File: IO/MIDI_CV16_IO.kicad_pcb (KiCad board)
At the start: 2 copper layers, 59.5 x 99.5 mm, 111 parts, among them J1 Conn_01x08_Male, J10 AudioJack2_SwitchT, J11 Conn_01x10_Male, J12 AudioJack2_SwitchT, J13 AudioJack2_SwitchT, J14 AudioJack2_SwitchT, J15 AudioJack2_SwitchT, J16 AudioJack2_SwitchT, J17 AudioJack2_SwitchT, J18 AudioJack2_SwitchT, J19 AudioJack2_SwitchT, J2 Conn_01x08_Male, J20 Conn_01x10_Male, J3 AudioJack2_SwitchT, J4 AudioJack2_SwitchT, J5 AudioJack2_SwitchT, J6 AudioJack2_SwitchT, J7 AudioJack2_SwitchT, J8 AudioJack2_SwitchT, J9 AudioJack2_SwitchT, SW1 SW_SPST, SW2 SW_SPST, SW3 SW_SPST

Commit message: Fix DRC errors
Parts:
- D1, D2, D21, D22, D23, D24, D25, D26, D27, D28, D29, D3, D30, D31, D32, D33, D34, D35, D36, D37, D38, D39, D4, D40, D41, D42, D43, D44, D45, D46, D47, D48, D49, D50, D51, D52, D53, D54, D55, D56: footprint LED_THT:LED_D3.0mm -> Custom_FP:LED_D3.0mm_NoCourtyard
- J1, J2: value Conn_01x08_Male -> Conn_01x10_Male
- J10, J12, J13, J14, J15, J16, J17, J18, J19, J3, J4, J5, J6, J7, J8, J9: footprint CustomLib:PJ398SM -> Custom_FP:PJ398SM

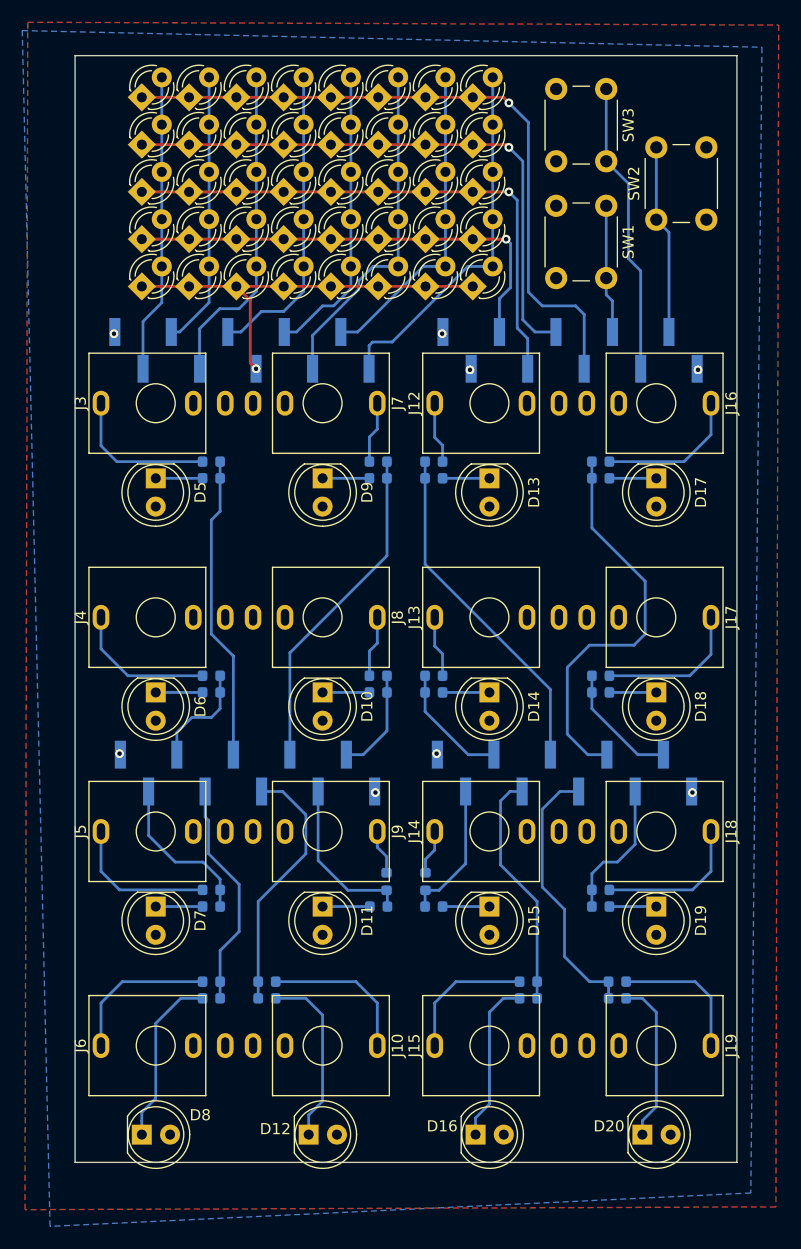
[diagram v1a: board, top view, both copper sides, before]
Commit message: Update to KiCAD 7
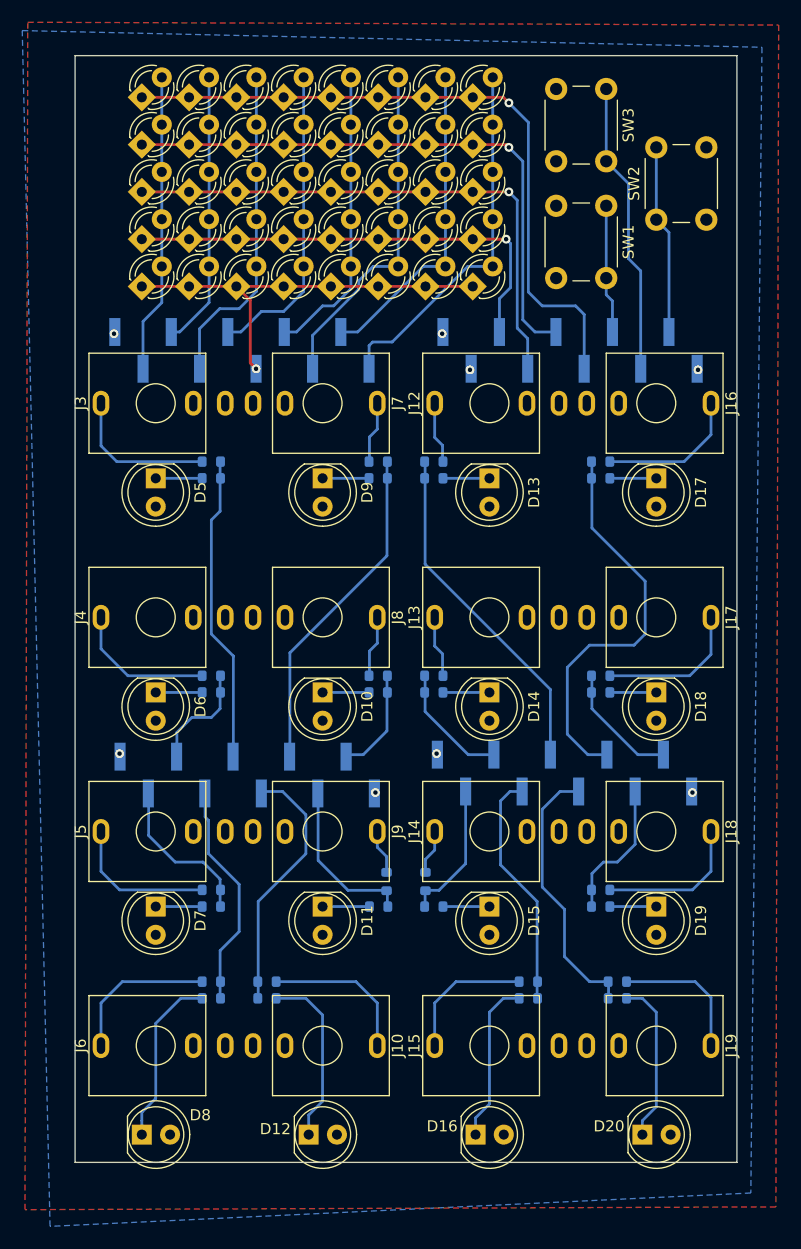
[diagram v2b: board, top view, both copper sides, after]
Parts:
- moved J11 0.18 mm to (54.0, 130.2)
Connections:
- J10 pad TN: (no net) -> unconnected-(J10-PadTN)
- J12 pad TN: (no net) -> unconnected-(J12-PadTN)
- J13 pad TN: (no net) -> unconnected-(J13-PadTN)
- J14 pad TN: (no net) -> unconnected-(J14-PadTN)
- J15 pad TN: (no net) -> unconnected-(J15-PadTN)
- J16 pad TN: (no net) -> unconnected-(J16-PadTN)
- J17 pad TN: (no net) -> unconnected-(J17-PadTN)
- J18 pad TN: (no net) -> unconnected-(J18-PadTN)
- J19 pad TN: (no net) -> unconnected-(J19-PadTN)
- J3 pad TN: (no net) -> unconnected-(J3-PadTN)
- J4 pad TN: (no net) -> unconnected-(J4-PadTN)
- J5 pad TN: (no net) -> unconnected-(J5-PadTN)
- J6 pad TN: (no net) -> unconnected-(J6-PadTN)
- J7 pad TN: (no net) -> unconnected-(J7-PadTN)
- J8 pad TN: (no net) -> unconnected-(J8-PadTN)
- J9 pad TN: (no net) -> unconnected-(J9-PadTN)
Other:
- net class Default removed

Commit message: Update PCBs to V3.0
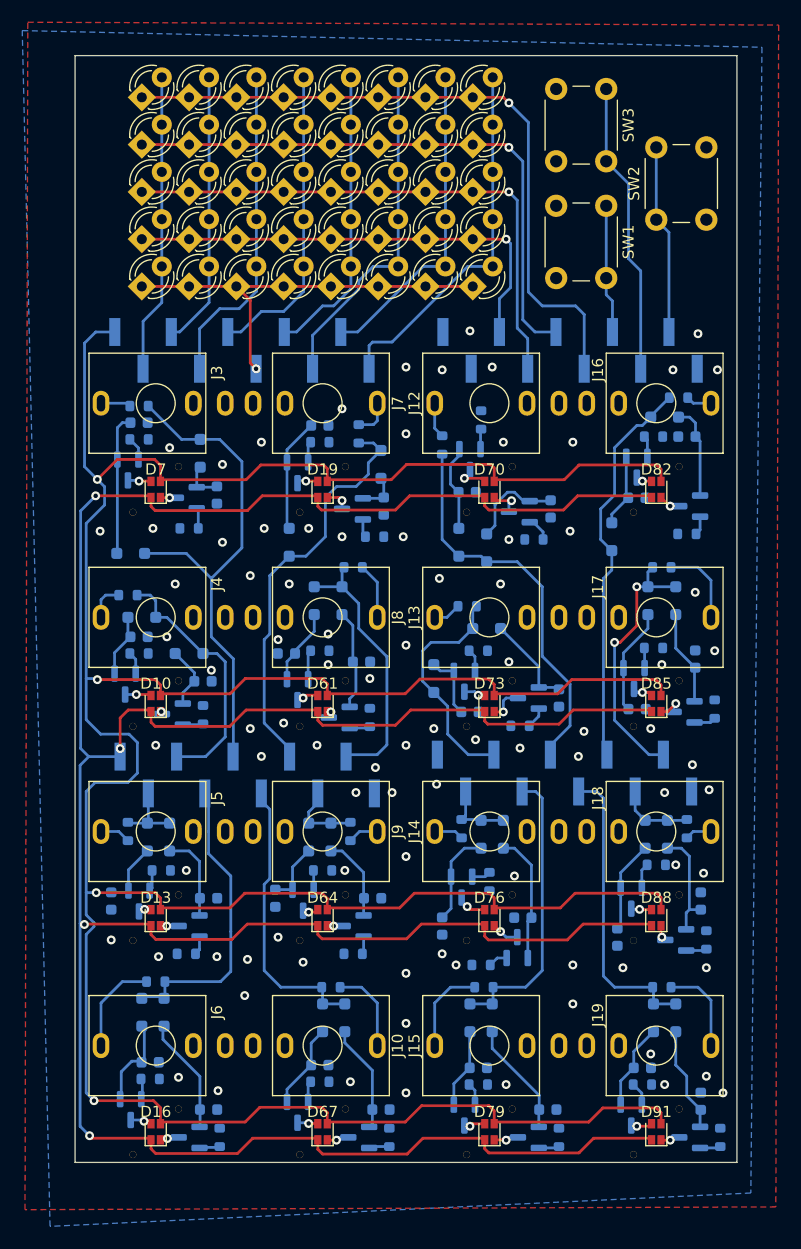
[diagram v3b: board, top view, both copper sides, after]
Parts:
- added C10: 100pF, Capacitor_SMD:C_0603_1608Metric, B.Cu at (45.2, 156.0)
- added C11: 100pF, Capacitor_SMD:C_0603_1608Metric, B.Cu at (66.2, 106.0)
- added C12: 100pF, Capacitor_SMD:C_0603_1608Metric, B.Cu at (60.5, 98.8)
- added C13: 100pF, Capacitor_SMD:C_0603_1608Metric, B.Cu at (64.2, 120.0)
- added C14: 100pF, Capacitor_SMD:C_0603_1608Metric, B.Cu at (57.5, 119.2)
- added C15: 100pF, Capacitor_SMD:C_0603_1608Metric, B.Cu at (65.2, 141.2)
- added C16: 100pF, Capacitor_SMD:C_0603_1608Metric, B.Cu at (56.5, 141.2)
- added C17: 100pF, Capacitor_SMD:C_0603_1608Metric, B.Cu at (66.0, 160.2)
- added C18: 100pF, Capacitor_SMD:C_0603_1608Metric, B.Cu at (60.5, 156.2)
- added C19: 100pF, Capacitor_SMD:C_0603_1608Metric, B.Cu at (81.2, 106.2)
- added C20: 100pF, Capacitor_SMD:C_0603_1608Metric, B.Cu at (73.8, 104.8)
- added C21: 100pF, Capacitor_SMD:C_0603_1608Metric, B.Cu at (82.0, 123.2)
- added C22: 100pF, Capacitor_SMD:C_0603_1608Metric, B.Cu at (74.0, 124.5)
- added C23: 100pF, Capacitor_SMD:C_0603_1608Metric, B.Cu at (78.8, 143.0)
- added C24: 100pF, Capacitor_SMD:C_0603_1608Metric, B.Cu at (71.5, 143.8)
- added C25: 100pF, Capacitor_SMD:C_0603_1608Metric, B.Cu at (81.0, 160.2)
- added C26: 100pF, Capacitor_SMD:C_0603_1608Metric, B.Cu at (74.8, 156.5)
- added C27: 100pF, Capacitor_SMD:C_0603_1608Metric, B.Cu at (93.5, 99.8)
- added C28: 100pF, Capacitor_SMD:C_0603_1608Metric, B.Cu at (89.0, 105.2)
- added C29: 100pF, Capacitor_SMD:C_0603_1608Metric, B.Cu at (94.2, 119.8)
- added C3: 100pF, Capacitor_SMD:C_0603_1608Metric, B.Cu at (51.2, 105.0)
- added C30: 100pF, Capacitor_SMD:C_0603_1608Metric, B.Cu at (89.0, 124.2)
- added C31: 100pF, Capacitor_SMD:C_0603_1608Metric, B.Cu at (94.8, 141.5)
- added C32: 100pF, Capacitor_SMD:C_0603_1608Metric, B.Cu at (87.2, 144.8)
- added C33: 100pF, Capacitor_SMD:C_0603_1608Metric, B.Cu at (94.8, 159.5)
- added C34: 100pF, Capacitor_SMD:C_0603_1608Metric, B.Cu at (89.5, 156.5)
- added C4: 100pF, Capacitor_SMD:C_0603_1608Metric, B.Cu at (44.2, 98.5)
- added C5: 100pF, Capacitor_SMD:C_0603_1608Metric, B.Cu at (50.0, 121.8)
- added C6: 100pF, Capacitor_SMD:C_0603_1608Metric, B.Cu at (44.2, 117.8)
- added C7: 100pF, Capacitor_SMD:C_0603_1608Metric, B.Cu at (50.5, 141.2)
- added C8: 100pF, Capacitor_SMD:C_0603_1608Metric, B.Cu at (41.8, 141.5)
- added C9: 100pF, Capacitor_SMD:C_0603_1608Metric, B.Cu at (50.5, 160.2)
- added D60: SD103, Diode_SMD:D_SOD-323_HandSoldering, B.Cu at (60.0, 114.5)
- added D61: LED_Dual_AAKK, Custom_FP:LED_LiteOn_LTST-C195TGKRKT, F.Cu at (60.8, 123.8)
- added D62: SD103, Diode_SMD:D_SOD-323_HandSoldering, B.Cu at (61.5, 135.8)
- added D63: SD103, Diode_SMD:D_SOD-323_HandSoldering, B.Cu at (59.5, 135.8)
- added D64: LED_Dual_AAKK, Custom_FP:LED_LiteOn_LTST-C195TGKRKT, F.Cu at (60.8, 143.0)
- added D65: SD103, Diode_SMD:D_SOD-323_HandSoldering, B.Cu at (62.8, 152.0)
- added D66: SD103, Diode_SMD:D_SOD-323_HandSoldering, B.Cu at (60.8, 152.0)
- added D67: LED_Dual_AAKK, Custom_FP:LED_LiteOn_LTST-C195TGKRKT, F.Cu at (60.8, 162.2)
- added D68: SD103, Diode_SMD:D_SOD-323_HandSoldering, B.Cu at (75.5, 109.8)
- added D69: SD103, Diode_SMD:D_SOD-323_HandSoldering, B.Cu at (73.0, 109.2)
- added D70: LED_Dual_AAKK, Custom_FP:LED_LiteOn_LTST-C195TGKRKT, F.Cu at (75.8, 104.5)
- added D71: SD103, Diode_SMD:D_SOD-323_HandSoldering, B.Cu at (75.5, 117.0)
- added D72: SD103, Diode_SMD:D_SOD-323_HandSoldering, B.Cu at (70.8, 121.5)
- added D73: LED_Dual_AAKK, Custom_FP:LED_LiteOn_LTST-C195TGKRKT, F.Cu at (75.8, 123.8)
- added D74: SD103, Diode_SMD:D_SOD-323_HandSoldering, B.Cu at (77.0, 135.5)
- added D75: SD103, Diode_SMD:D_SOD-323_HandSoldering, B.Cu at (75.0, 135.5)
- added D76: LED_Dual_AAKK, Custom_FP:LED_LiteOn_LTST-C195TGKRKT, F.Cu at (75.8, 143.0)
- added D77: SD103, Diode_SMD:D_SOD-323_HandSoldering, B.Cu at (76.0, 152.0)
- added D78: SD103, Diode_SMD:D_SOD-323_HandSoldering, B.Cu at (74.0, 152.0)
- added D79: LED_Dual_AAKK, Custom_FP:LED_LiteOn_LTST-C195TGKRKT, F.Cu at (75.8, 162.2)
- added D80: SD103, Diode_SMD:D_SOD-323_HandSoldering, B.Cu at (91.5, 98.0)
- added D81: SD103, Diode_SMD:D_SOD-323_HandSoldering, B.Cu at (86.8, 108.8)
- added D82: LED_Dual_AAKK, Custom_FP:LED_LiteOn_LTST-C195TGKRKT, F.Cu at (90.8, 104.5)
- added D83: SD103, Diode_SMD:D_SOD-323_HandSoldering, B.Cu at (92.5, 114.5)
- added D84: SD103, Diode_SMD:D_SOD-323_HandSoldering, B.Cu at (90.0, 114.5)
- added D85: LED_Dual_AAKK, Custom_FP:LED_LiteOn_LTST-C195TGKRKT, F.Cu at (90.8, 123.8)
- added D86: SD103, Diode_SMD:D_SOD-323_HandSoldering, B.Cu at (91.8, 135.5)
- added D87: SD103, Diode_SMD:D_SOD-323_HandSoldering, B.Cu at (89.8, 135.5)
- added D88: LED_Dual_AAKK, Custom_FP:LED_LiteOn_LTST-C195TGKRKT, F.Cu at (90.8, 143.0)
- added D89: SD103, Diode_SMD:D_SOD-323_HandSoldering, B.Cu at (92.5, 152.0)
- added D90: SD103, Diode_SMD:D_SOD-323_HandSoldering, B.Cu at (90.5, 152.0)
- added D91: LED_Dual_AAKK, Custom_FP:LED_LiteOn_LTST-C195TGKRKT, F.Cu at (90.8, 162.2)
- added H1: MountingHole, Custom_FP:VLP-LightPipes, F.Cu at (45.8, 104.5)
- added H10: MountingHole, Custom_FP:VLP-LightPipes, F.Cu at (75.8, 123.8)
- added H11: MountingHole, Custom_FP:VLP-LightPipes, F.Cu at (75.8, 143.0)
- added H12: MountingHole, Custom_FP:VLP-LightPipes, F.Cu at (75.8, 162.2)
- added H13: MountingHole, Custom_FP:VLP-LightPipes, F.Cu at (90.8, 104.5)
- added H14: MountingHole, Custom_FP:VLP-LightPipes, F.Cu at (90.8, 123.8)
- added H15: MountingHole, Custom_FP:VLP-LightPipes, F.Cu at (90.8, 143.0)
- added H16: MountingHole, Custom_FP:VLP-LightPipes, F.Cu at (90.8, 162.2)
- added H2: MountingHole, Custom_FP:VLP-LightPipes, F.Cu at (45.8, 123.8)
- added H3: MountingHole, Custom_FP:VLP-LightPipes, F.Cu at (45.8, 143.0)
- added H4: MountingHole, Custom_FP:VLP-LightPipes, F.Cu at (45.8, 162.2)
- added H5: MountingHole, Custom_FP:VLP-LightPipes, F.Cu at (60.8, 104.5)
- added H6: MountingHole, Custom_FP:VLP-LightPipes, F.Cu at (60.8, 123.8)
- added H7: MountingHole, Custom_FP:VLP-LightPipes, F.Cu at (60.8, 143.0)
- added H8: MountingHole, Custom_FP:VLP-LightPipes, F.Cu at (60.8, 162.2)
- added H9: MountingHole, Custom_FP:VLP-LightPipes, F.Cu at (75.8, 104.5)
- added Q10: BC847C, Package_TO_SOT_SMD:SOT-23, B.Cu at (48.8, 162.8)
- added Q11: BC857C, Package_TO_SOT_SMD:SOT-23, B.Cu at (58.5, 103.0)
- added Q12: BC847C, Package_TO_SOT_SMD:SOT-23, B.Cu at (63.4, 106.2)
- added Q13: BC857C, Package_TO_SOT_SMD:SOT-23, B.Cu at (58.5, 122.5)
- added Q14: BC847C, Package_TO_SOT_SMD:SOT-23, B.Cu at (62.2, 125.0)
- added Q15: BC857C, Package_TO_SOT_SMD:SOT-23, B.Cu at (59.0, 141.4)
- added Q16: BC847C, Package_TO_SOT_SMD:SOT-23, B.Cu at (63.5, 143.8)
- added Q17: BC857C, Package_TO_SOT_SMD:SOT-23, B.Cu at (58.5, 160.5)
- added Q18: BC847C, Package_TO_SOT_SMD:SOT-23, B.Cu at (64.0, 162.8)
- added Q19: BC857C, Package_TO_SOT_SMD:SOT-23, B.Cu at (74.0, 101.8)
- added Q20: BC847C, Package_TO_SOT_SMD:SOT-23, B.Cu at (78.4, 106.5)
- added Q21: BC857C, Package_TO_SOT_SMD:SOT-23, B.Cu at (73.5, 121.8)
- added Q22: BC847C, Package_TO_SOT_SMD:SOT-23, B.Cu at (79.2, 123.2)
- added Q23: BC857C, Package_TO_SOT_SMD:SOT-23, B.Cu at (73.2, 140.2)
- added Q24: BC847C, Package_TO_SOT_SMD:SOT-23, B.Cu at (78.2, 145.7)
- added Q25: BC857C, Package_TO_SOT_SMD:SOT-23, B.Cu at (73.5, 160.8)
- added Q26: BC847C, Package_TO_SOT_SMD:SOT-23, B.Cu at (79.2, 162.8)
- added Q27: BC857C, Package_TO_SOT_SMD:SOT-23, B.Cu at (89.0, 102.5)
- added Q28: BC847C, Package_TO_SOT_SMD:SOT-23, B.Cu at (93.8, 106.0)
- added Q29: BC857C, Package_TO_SOT_SMD:SOT-23, B.Cu at (88.8, 121.5)
- added Q3: BC857C, Package_TO_SOT_SMD:SOT-23, B.Cu at (43.2, 102.8)
- added Q30: BC847C, Package_TO_SOT_SMD:SOT-23, B.Cu at (93.2, 124.5)
- added Q31: BC857C, Package_TO_SOT_SMD:SOT-23, B.Cu at (88.5, 141.2)
- added Q32: BC847C, Package_TO_SOT_SMD:SOT-23, B.Cu at (92.5, 145.0)
- added Q33: BC857C, Package_TO_SOT_SMD:SOT-23, B.Cu at (88.5, 160.8)
- added Q34: BC847C, Package_TO_SOT_SMD:SOT-23, B.Cu at (93.8, 162.8)
- added Q4: BC847C, Package_TO_SOT_SMD:SOT-23, B.Cu at (48.5, 105.2)
- added Q5: BC857C, Package_TO_SOT_SMD:SOT-23, B.Cu at (43.0, 122.0)
- added Q6: BC847C, Package_TO_SOT_SMD:SOT-23, B.Cu at (47.2, 124.7)
- added Q7: BC857C, Package_TO_SOT_SMD:SOT-23, B.Cu at (44.2, 141.5)
- added Q8: BC847C, Package_TO_SOT_SMD:SOT-23, B.Cu at (48.8, 143.8)
- added Q9: BC857C, Package_TO_SOT_SMD:SOT-23, B.Cu at (43.5, 160.2)
- added R37: 2k, Resistor_SMD:R_0603_1608Metric, B.Cu at (74.8, 158.0)
- added R38: 2k, Resistor_SMD:R_0603_1608Metric, B.Cu at (82.0, 162.8)
- added R39: 1k, Resistor_SMD:R_0603_1608Metric, B.Cu at (75.2, 149.2)
- added R4: 2k, Resistor_SMD:R_0603_1608Metric, B.Cu at (44.2, 100.0)
- added R40: 2k, Resistor_SMD:R_0603_1608Metric, B.Cu at (90.5, 99.8)
- added R41: 2k, Resistor_SMD:R_0603_1608Metric, B.Cu at (93.5, 108.5)
- added R42: 1k, Resistor_SMD:R_0603_1608Metric, B.Cu at (92.8, 96.2)
- added R43: 2k, Resistor_SMD:R_0603_1608Metric, B.Cu at (90.5, 118.8)
- added R44: 2k, Resistor_SMD:R_0603_1608Metric, B.Cu at (96.0, 124.2)
- added R45: 1k, Resistor_SMD:R_0603_1608Metric, B.Cu at (91.2, 111.5)
- added R46: 2k, Resistor_SMD:R_0603_1608Metric, B.Cu at (90.8, 138.2)
- added R47: 2k, Resistor_SMD:R_0603_1608Metric, B.Cu at (95.2, 145.0)
- added R48: 1k, Resistor_SMD:R_0603_1608Metric, B.Cu at (93.5, 135.0)
- added R49: 2k, Resistor_SMD:R_0603_1608Metric, B.Cu at (89.5, 158.0)
- added R50: 2k, Resistor_SMD:R_0603_1608Metric, B.Cu at (96.5, 162.8)
- added R51: 1k, Resistor_SMD:R_0603_1608Metric, B.Cu at (91.2, 149.2)
- D10, D13, D16, D19, D7: value LED_RG -> LED_Dual_AAKK; footprint LED_THT:LED_D5.0mm_FlatTop -> Custom_FP:LED_LiteOn_LTST-C195TGKRKT
- D11, D12, D14, D15, D17, D18, D20, D5, D6, D8, D9: value LED_RG -> SD103; footprint LED_THT:LED_D5.0mm_FlatTop -> Diode_SMD:D_SOD-323_HandSoldering; moved to B.Cu
- R10, R11, R13, R14, R16, R17, R19, R20, R22, R23, R25, R26, R28, R29, R31, R32, R34, R35, R5, R7, R8: value 1k -> 2k
- moved R25 59.8 mm to (60.5, 157.8)
- moved R13 55.8 mm to (45.2, 157.5)
- moved D20 55.1 mm to (62.5, 114.5), turned to 90 degrees
- moved R28 53.4 mm to (75.0, 98.2), turned to -90 degrees
- moved D13 49.6 mm to (45.8, 143.0), turned to 0 degrees
- moved R16 49.5 mm to (60.5, 100.2)
- moved D19 48.0 mm to (60.8, 104.5), turned to 0 degrees
- moved R26 44.3 mm to (66.8, 162.8), turned to 90 degrees
- moved D8 43.5 mm to (48.8, 119.2)
- moved R14 41.5 mm to (51.5, 162.8), turned to 90 degrees
- moved D14 41.0 mm to (46.5, 151.5), turned to 90 degrees
- moved D7 37.5 mm to (45.8, 104.5), turned to 0 degrees
- moved D18 35.7 mm to (57.8, 109.2), turned to 90 degrees
- moved D15 32.7 mm to (44.5, 151.5)
- moved D12 30.4 mm to (45.0, 135.8), turned to -90 degrees
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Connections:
- D10 pad 1: Net-(D10-KA) -> +VDC
- D10 pad 2: GND1 -> Net-(D10-A2)
- D11 pad 1: Net-(D11-KA) -> Net-(D11-K)
- D11 pad 2: GND1 -> /Outputs3/In
- D12 pad 1: Net-(D12-KA) -> /Outputs3/In
- D12 pad 2: GND1 -> Net-(D12-A)
- D13 pad 1: Net-(D13-KA) -> +VDC
- D13 pad 2: GND1 -> Net-(D13-A2)
- D14 pad 1: Net-(D14-KA) -> Net-(D14-K)
- D14 pad 2: GND1 -> /Outputs4/In
- D15 pad 1: Net-(D15-KA) -> /Outputs4/In
- D15 pad 2: GND1 -> Net-(D15-A)
- D16 pad 1: Net-(D16-KA) -> +VDC
- D16 pad 2: GND1 -> Net-(D16-A2)
- D17 pad 1: Net-(D17-KA) -> Net-(D17-K)
- D17 pad 2: GND1 -> /Outputs5/In
- D18 pad 1: Net-(D18-KA) -> /Outputs5/In
- D18 pad 2: GND1 -> Net-(D18-A)
- D19 pad 1: Net-(D19-KA) -> +VDC
- D19 pad 2: GND1 -> Net-(D19-A2)
- D20 pad 1: Net-(D20-KA) -> Net-(D20-K)
- D20 pad 2: GND1 -> /Outputs6/In
- D5 pad 1: Net-(D5-KA) -> Net-(D5-K)
- D5 pad 2: GND1 -> /Outputs1/In
- D6 pad 1: Net-(D6-KA) -> /Outputs1/In
- D6 pad 2: GND1 -> Net-(D6-A)
- D7 pad 1: Net-(D7-KA) -> +VDC
- D7 pad 2: GND1 -> Net-(D7-A2)
- D8 pad 1: Net-(D8-KA) -> Net-(D8-K)
- D8 pad 2: GND1 -> /Outputs2/In
- D9 pad 1: Net-(D9-KA) -> /Outputs2/In
- D9 pad 2: GND1 -> Net-(D9-A)
- J1 pad 1: GND1 -> GND
- J1 pad 10: GND1 -> GND
- J1 pad 9: GND1 -> GND
- J10 pad S: GND1 -> GND
- J11 pad 1: GND1 -> -VDC
- J11 pad 10: GND1 -> GND
- J11 pad 2: Net-(J11-Pin_2) -> /Outputs3/In
- J11 pad 3: Net-(J11-Pin_3) -> /Outputs2/In
- J11 pad 4: Net-(J11-Pin_4) -> /Outputs4/In
- J11 pad 5: Net-(J11-Pin_5) -> /Outputs1/In
- J11 pad 6: Net-(J11-Pin_6) -> /Outputs8/In
- J11 pad 7: Net-(J11-Pin_7) -> /Outputs5/In
- J11 pad 8: Net-(J11-Pin_8) -> /Outputs7/In
- J11 pad 9: Net-(J11-Pin_9) -> /Outputs6/In
- J12 pad S: GND1 -> GND
- J13 pad S: GND1 -> GND
- J14 pad S: GND1 -> GND
- J15 pad S: GND1 -> GND
- J16 pad S: GND1 -> GND
- J17 pad S: GND1 -> GND
- J18 pad S: GND1 -> GND
- J19 pad S: GND1 -> GND
- J2 pad 10: GND1 -> +VDC
- J20 pad 1: GND1 -> GND
- J20 pad 10: GND1 -> GND
- J20 pad 2: Net-(J20-Pin_2) -> /Outputs11/In
- J20 pad 3: Net-(J20-Pin_3) -> /Outputs10/In
- J20 pad 4: Net-(J20-Pin_4) -> /Outputs12/In
- J20 pad 5: Net-(J20-Pin_5) -> /Outputs9/In
- J20 pad 6: Net-(J20-Pin_6) -> /Outputs16/In
- J20 pad 7: Net-(J20-Pin_7) -> /Outputs13/In
- J20 pad 8: Net-(J20-Pin_8) -> /Outputs15/In
- J20 pad 9: Net-(J20-Pin_9) -> /Outputs14/In
- J3 pad S: GND1 -> GND
- J4 pad S: GND1 -> GND
- J5 pad S: GND1 -> GND
- J6 pad S: GND1 -> GND
- J7 pad S: GND1 -> GND
- J8 pad S: GND1 -> GND
- J9 pad S: GND1 -> GND
- R10 pad 1: Net-(D10-KA) -> GND
- R10 pad 2: Net-(J11-Pin_9) -> Net-(Q7-E)
- R11 pad 1: Net-(D11-KA) -> Net-(Q8-E)
- R11 pad 2: Net-(J11-Pin_8) -> GND
- R12 pad 1: Net-(D12-KA) -> /Outputs3/In
- R12 pad 2: Net-(J11-Pin_6) -> Net-(J5-PadT)
- R13 pad 1: Net-(J11-Pin_5) -> GND
- R13 pad 2: Net-(J3-PadT) -> Net-(Q9-E)
- R14 pad 1: Net-(J11-Pin_3) -> Net-(Q10-E)
- R14 pad 2: Net-(J4-PadT) -> GND
- R15 pad 1: Net-(J11-Pin_2) -> /Outputs4/In
- R15 pad 2: Net-(J5-PadT) -> Net-(J6-PadT)
- R16 pad 1: Net-(J11-Pin_4) -> GND
- R16 pad 2: Net-(J6-PadT) -> Net-(Q11-E)
- R17 pad 1: Net-(J11-Pin_7) -> Net-(Q12-E)
- R17 pad 2: Net-(J7-PadT) -> GND
- R18 pad 1: Net-(J11-Pin_9) -> /Outputs5/In
- R18 pad 2: Net-(J8-PadT) -> Net-(J7-PadT)
- R19 pad 1: Net-(J11-Pin_8) -> GND
- R19 pad 2: Net-(J9-PadT) -> Net-(Q13-E)
- R20 pad 1: Net-(J11-Pin_6) -> Net-(Q14-E)
- R20 pad 2: Net-(J10-PadT) -> GND
- R21 pad 1: Net-(D13-KA) -> /Outputs6/In
- R21 pad 2: Net-(J20-Pin_5) -> Net-(J8-PadT)
- R22 pad 1: Net-(D14-KA) -> GND
- R22 pad 2: Net-(J20-Pin_3) -> Net-(Q15-E)
- R23 pad 1: Net-(D15-KA) -> Net-(Q16-E)
- R23 pad 2: Net-(J20-Pin_2) -> GND
- R24 pad 1: Net-(D16-KA) -> /Outputs7/In
- R24 pad 2: Net-(J20-Pin_4) -> Net-(J9-PadT)
- R25 pad 1: Net-(D17-KA) -> GND
- R25 pad 2: Net-(J20-Pin_7) -> Net-(Q17-E)
- R26 pad 1: Net-(D18-KA) -> Net-(Q18-E)
- R26 pad 2: Net-(J20-Pin_9) -> GND
- R27 pad 1: Net-(D19-KA) -> /Outputs8/In
- R27 pad 2: Net-(J20-Pin_8) -> Net-(J10-PadT)
- R28 pad 1: Net-(D20-KA) -> GND
- R28 pad 2: Net-(J20-Pin_6) -> Net-(Q19-E)
- R29 pad 1: Net-(J20-Pin_5) -> Net-(Q20-E)
- R29 pad 2: Net-(J12-PadT) -> GND
- R30 pad 1: Net-(J20-Pin_3) -> /Outputs9/In
- R30 pad 2: Net-(J13-PadT) -> Net-(J12-PadT)
- R31 pad 1: Net-(J20-Pin_2) -> GND
- R31 pad 2: Net-(J14-PadT) -> Net-(Q21-E)
- R32 pad 1: Net-(J20-Pin_4) -> Net-(Q22-E)
- R32 pad 2: Net-(J15-PadT) -> GND
- R33 pad 1: Net-(J20-Pin_7) -> /Outputs10/In
- R33 pad 2: Net-(J16-PadT) -> Net-(J13-PadT)
- R34 pad 1: Net-(J20-Pin_9) -> GND
- R34 pad 2: Net-(J17-PadT) -> Net-(Q23-E)
- R35 pad 1: Net-(J20-Pin_8) -> Net-(Q24-E)
- R35 pad 2: Net-(J18-PadT) -> GND
- R36 pad 1: Net-(J20-Pin_6) -> /Outputs11/In
- R36 pad 2: Net-(J19-PadT) -> Net-(J14-PadT)
- R5 pad 1: Net-(D5-KA) -> Net-(Q4-E)
- R5 pad 2: Net-(J11-Pin_5) -> GND
- R6 pad 1: Net-(D6-KA) -> /Outputs1/In
- R6 pad 2: Net-(J11-Pin_3) -> Net-(J3-PadT)
- R7 pad 1: Net-(D7-KA) -> GND
- R7 pad 2: Net-(J11-Pin_2) -> Net-(Q5-E)
- R8 pad 1: Net-(D8-KA) -> Net-(Q6-E)
- R8 pad 2: Net-(J11-Pin_4) -> GND
- R9 pad 1: Net-(D9-KA) -> /Outputs2/In
- R9 pad 2: Net-(J11-Pin_7) -> Net-(J4-PadT)
- SW1 pad 2: GND1 -> GND
- SW2 pad 2: GND1 -> GND
- SW3 pad 2: GND1 -> GND
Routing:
- net +VDC: track 0.00 -> 311.2 mm, vias 0 -> 4
- net -VDC: track 0.00 -> 285.8 mm, vias 0 -> 4
- net /Outputs1/In: track 0.00 -> 45.7 mm
- net /Outputs5/In: track 0.00 -> 37.0 mm
- net Net-(J20-Pin_7): track 36.0 -> 0.00 mm
- net /Outputs13/In: track 0.00 -> 35.8 mm
- net /Outputs9/In: track 0.00 -> 35.3 mm
- net Net-(J20-Pin_5): track 31.0 -> 0.00 mm
- net Net-(J11-Pin_7): track 30.0 -> 0.00 mm
- net Net-(J11-Pin_5): track 27.5 -> 0.00 mm
- net /Outputs16/In: track 0.00 -> 26.8 mm
- net /Outputs4/In: track 0.00 -> 26.8 mm
- net /Outputs12/In: track 0.00 -> 26.1 mm
- net /Outputs8/In: track 0.00 -> 25.8 mm
- net Net-(J20-Pin_6): track 24.4 -> 0.00 mm
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- added copper zone on B.Cu, net GND
- added copper zone on F.Cu, net GND
- removed copper zone on B.Cu, net GND1
- removed copper zone on F.Cu, net GND1

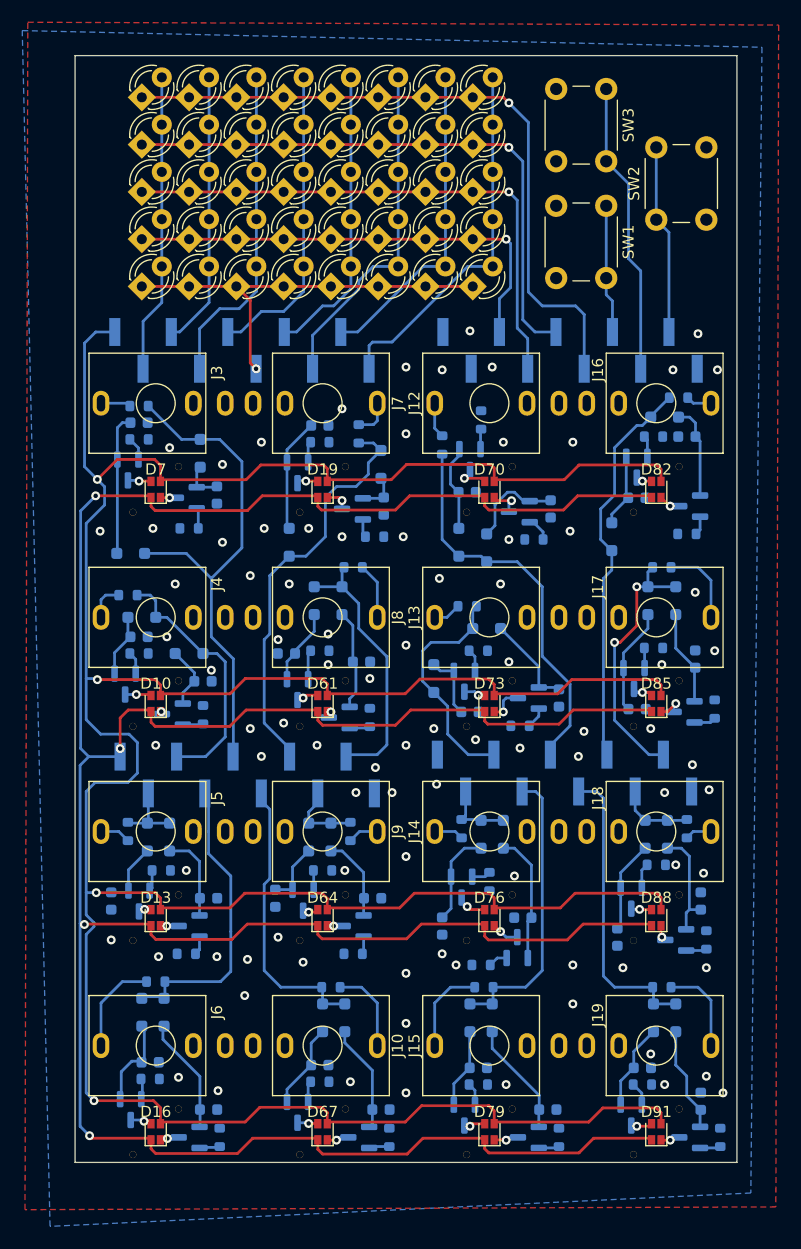
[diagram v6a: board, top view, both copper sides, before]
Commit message: Remove IO peak-detectors
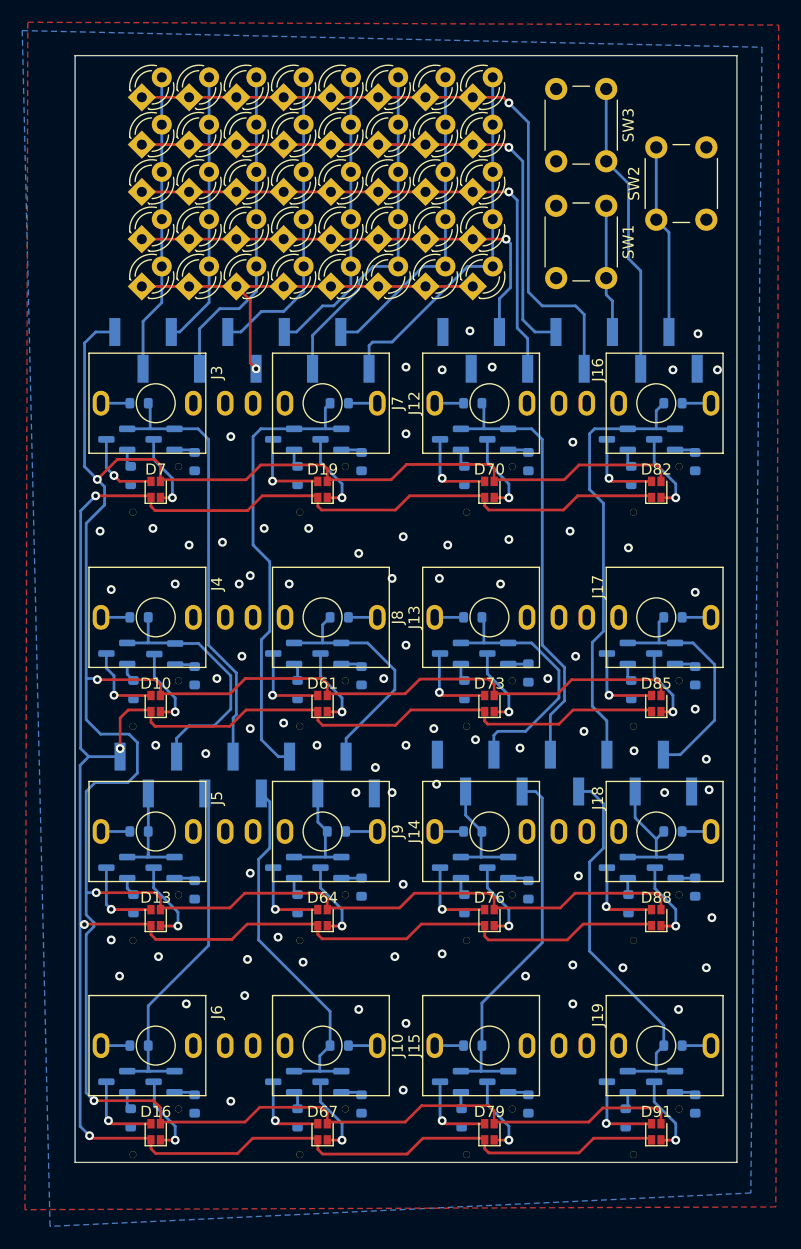
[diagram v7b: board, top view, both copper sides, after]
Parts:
- removed C10, C11, C12, C13, C14, C15, C16, C17, C18, C19, C20, C21, C22, C23, C24, C25, C26, C27, C28, C29, C3, C30, C31, C32, C33, C34, C4, C5, C6, C7, C8, C9: 100pF, Capacitor_SMD:C_0603_1608Metric
- removed D11, D12, D14, D15, D17, D18, D20, D5, D6, D60, D62, D63, D65, D66, D68, D69, D71, D72, D74, D75, D77, D78, D8, D80, D81, D83, D84, D86, D87, D89, D9, D90: SD103, Diode_SMD:D_SOD-323_HandSoldering
- D10, D13, D16, D19, D61, D64, D67, D7, D70, D73, D76, D79, D82, D85, D88, D91: value LED_Dual_AAKK -> LTST-C195TGKRKT
- H1, H10, H11, H12, H13, H14, H15, H16, H2, H3, H4, H5, H6, H7, H8, H9: value MountingHole -> VLP lightpipe
- moved R35 7.98 mm to (79.2, 140.5), turned to -90 degrees
- moved Q24 7.40 mm to (76.5, 138.5), turned to 180 degrees
- moved R29 7.02 mm to (79.2, 102.0), turned to -90 degrees
- moved R17 6.85 mm to (64.2, 102.0), turned to -90 degrees
- moved Q20 6.78 mm to (76.5, 100.0)
- moved Q32 6.57 mm to (91.6, 138.5)
- moved Q12 6.54 mm to (61.5, 100.0)
- moved R41 6.54 mm to (94.2, 102.0), turned to -90 degrees
- moved Q28 6.41 mm to (91.5, 100.0)
- moved R23 6.05 mm to (64.2, 140.2), turned to -90 degrees
- moved R5 6.02 mm to (49.2, 102.0), turned to -90 degrees
- moved R15 5.94 mm to (44.2, 154.5)
- moved Q14 5.80 mm to (61.5, 119.2)
- moved R11 5.80 mm to (49.2, 140.5), turned to -90 degrees
- moved Q8 5.71 mm to (46.5, 138.5)
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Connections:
- Q10 pad 1: Net-(D14-K) -> /Outputs4/In
- Q11 pad 1: Net-(D18-A) -> /Outputs5/In
- Q12 pad 1: Net-(D17-K) -> /Outputs5/In
- Q13 pad 1: Net-(D60-A) -> /Outputs6/In
- Q14 pad 1: Net-(D20-K) -> /Outputs6/In
- Q15 pad 1: Net-(D63-A) -> /Outputs7/In
- Q16 pad 1: Net-(D62-K) -> /Outputs7/In
- Q17 pad 1: Net-(D66-A) -> /Outputs8/In
- Q18 pad 1: Net-(D65-K) -> /Outputs8/In
- Q19 pad 1: Net-(D69-A) -> /Outputs9/In
- Q20 pad 1: Net-(D68-K) -> /Outputs9/In
- Q21 pad 1: Net-(D72-A) -> /Outputs10/In
- Q22 pad 1: Net-(D71-K) -> /Outputs10/In
- Q23 pad 1: Net-(D75-A) -> /Outputs11/In
- Q24 pad 1: Net-(D74-K) -> /Outputs11/In
- Q25 pad 1: Net-(D78-A) -> /Outputs12/In
- Q26 pad 1: Net-(D77-K) -> /Outputs12/In
- Q27 pad 1: Net-(D81-A) -> /Outputs13/In
- Q28 pad 1: Net-(D80-K) -> /Outputs13/In
- Q29 pad 1: Net-(D84-A) -> /Outputs14/In
- Q3 pad 1: Net-(D6-A) -> /Outputs1/In
- Q30 pad 1: Net-(D83-K) -> /Outputs14/In
- Q31 pad 1: Net-(D87-A) -> /Outputs15/In
- Q32 pad 1: Net-(D86-K) -> /Outputs15/In
- Q33 pad 1: Net-(D90-A) -> /Outputs16/In
- Q34 pad 1: Net-(D89-K) -> /Outputs16/In
- Q4 pad 1: Net-(D5-K) -> /Outputs1/In
- Q5 pad 1: Net-(D9-A) -> /Outputs2/In
- Q6 pad 1: Net-(D8-K) -> /Outputs2/In
- Q7 pad 1: Net-(D12-A) -> /Outputs3/In
- Q8 pad 1: Net-(D11-K) -> /Outputs3/In
- Q9 pad 1: Net-(D15-A) -> /Outputs4/In
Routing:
- net Net-(D6-A): track 12.7 -> 0.00 mm
- net Net-(D74-K): track 11.6 -> 0.00 mm
- net Net-(D14-K): track 10.5 -> 0.00 mm
- net Net-(D77-K): track 10.3 -> 0.00 mm
- net Net-(D18-A): track 10.2 -> 0.00 mm
- net Net-(D86-K): track 9.99 -> 0.00 mm
- net Net-(D65-K): track 9.69 -> 0.00 mm
- net Net-(D84-A): track 9.60 -> 0.00 mm
- net Net-(D89-K): track 9.51 -> 0.00 mm
- net Net-(D20-K): track 9.05 -> 0.00 mm
- net Net-(D68-K): track 8.76 -> 0.00 mm
- net Net-(D71-K): track 8.61 -> 0.00 mm
- net Net-(D75-A): track 8.55 -> 0.00 mm
- net Net-(D83-K): track 8.55 -> 0.00 mm
- net Net-(D80-K): track 8.44 -> 0.00 mm
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
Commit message: Layout v3.1
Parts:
- J1, J11, J2, J20: footprint Connector_PinHeader_2.54mm:PinHeader_1x10_P2.54mm_Vertical_SMD_Pin1Left -> Connector_PinHeader_2.54mm:PinHeader_1x10_P2.54mm_Vertical_SMD_Pin1Right
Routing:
- net Net-(D22-A): track 24.7 -> 28.7 mm
- net Net-(D37-A): track 26.6 -> 30.4 mm
- net /Outputs14/In: track 22.0 -> 25.5 mm
- net Net-(D47-A): track 28.8 -> 32.4 mm
- net /Outputs13/In: track 40.8 -> 44.1 mm
- net /Outputs2/In: track 23.5 -> 26.8 mm
- net Net-(J1-Pin_4): track 11.8 -> 15.1 mm
- net Net-(J1-Pin_3): track 26.4 -> 23.1 mm
- net Net-(J1-Pin_2): track 17.1 -> 20.4 mm
- net Net-(D32-A): track 27.6 -> 30.9 mm
- net Net-(D24-K): track 49.6 -> 46.3 mm
- net Net-(D21-K): track 37.9 -> 34.6 mm
- net Net-(D1-K): track 61.7 -> 58.4 mm
- net /Outputs9/In: track 39.8 -> 43.1 mm
- net /Outputs8/In: track 33.0 -> 36.3 mm
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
